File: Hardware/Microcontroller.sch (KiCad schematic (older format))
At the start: 28 parts

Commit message: Charger circuitry values
#26
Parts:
- removed C?: 4.7nF, symbol Capacitor
- removed D? (x2): TVS, symbol TVS
- removed R?: 1M, symbol Resistor
- removed RV? (x2): Varistor, symbol Varistor
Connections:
- net labels removed: GNDPWR
- wire segments 116 -> 77
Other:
- moved on the sheet: J?, PTC?

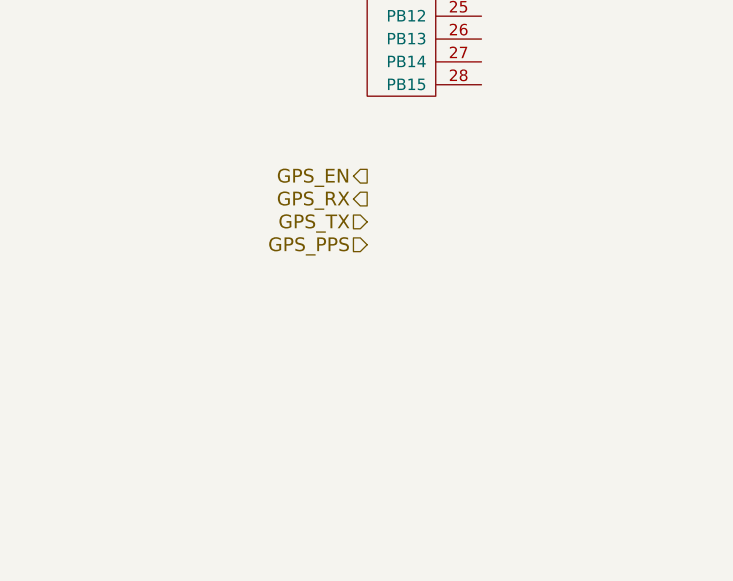
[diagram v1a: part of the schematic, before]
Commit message: Add solar charging capability
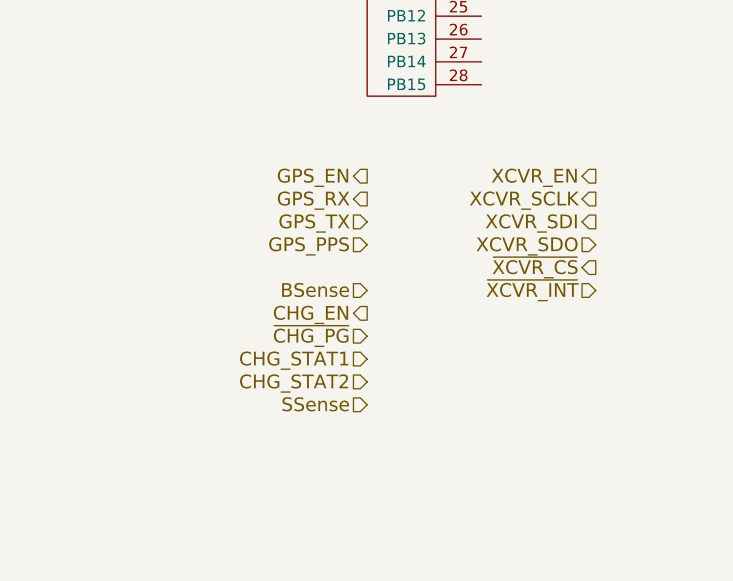
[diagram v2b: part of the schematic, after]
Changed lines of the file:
@@
 Wire Wire Line
 	4400 1400 4300 1400
+Text HLabel 8500 5500 0    60   Input ~ 0
+BSense
+Text HLabel 8500 5600 0    60   Output ~ 0
+CHG_EN
+Text HLabel 8500 5700 0    60   Input ~ 0
+~CHG_PG
+Text HLabel 8500 5800 0    60   Input ~ 0
+CHG_STAT1
+Text HLabel 8500 5900 0    60   Input ~ 0
+CHG_STAT2
+Text HLabel 9500 5000 0    60   Output ~ 0
+XCVR_EN
+Text HLabel 9500 5100 0    60   Output ~ 0
+XCVR_SCLK
+Text HLabel 9500 5200 0    60   Output ~ 0
+XCVR_SDI
+Text HLabel 9500 5300 0    60   Input ~ 0
+XCVR_SDO
+Text HLabel 9500 5400 0    60   Output ~ 0
+~XCVR_CS
+Text HLabel 9500 5500 0    60   Input ~ 0
+~XCVR_INT
+Text HLabel 8500 6000 0    60   Input ~ 0
+SSense
 $EndSCHEMATC

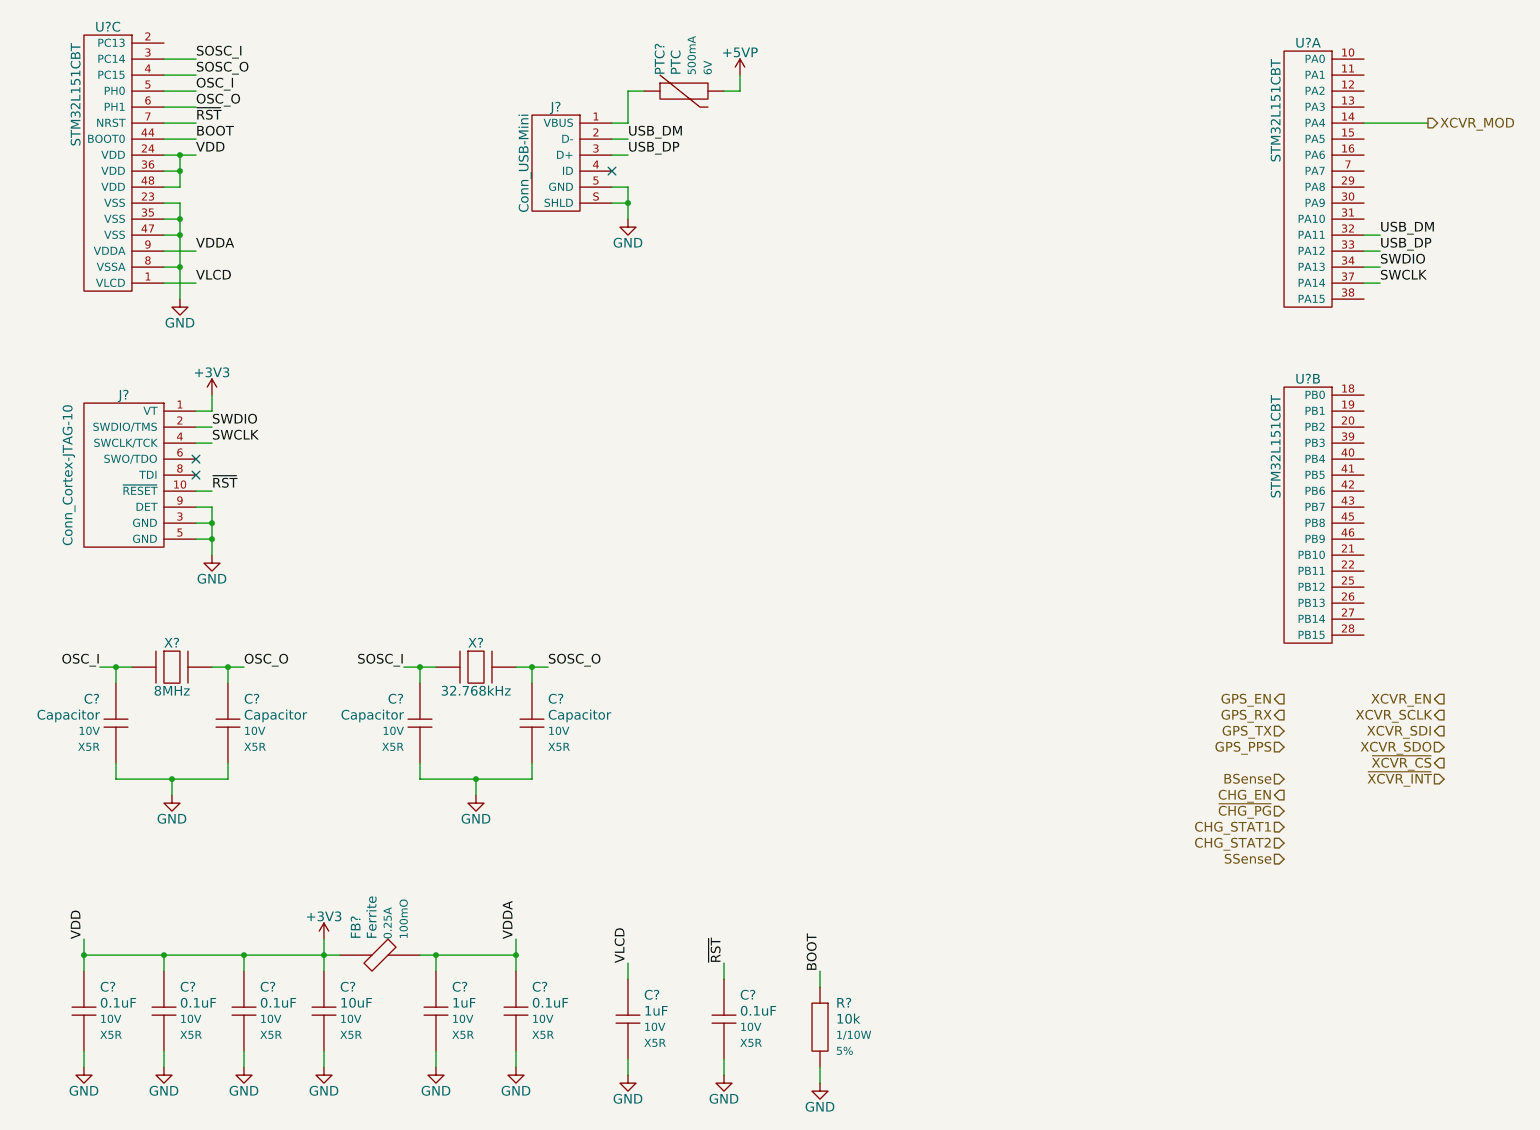
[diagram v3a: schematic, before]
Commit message: Oscillator selection
Closes #35
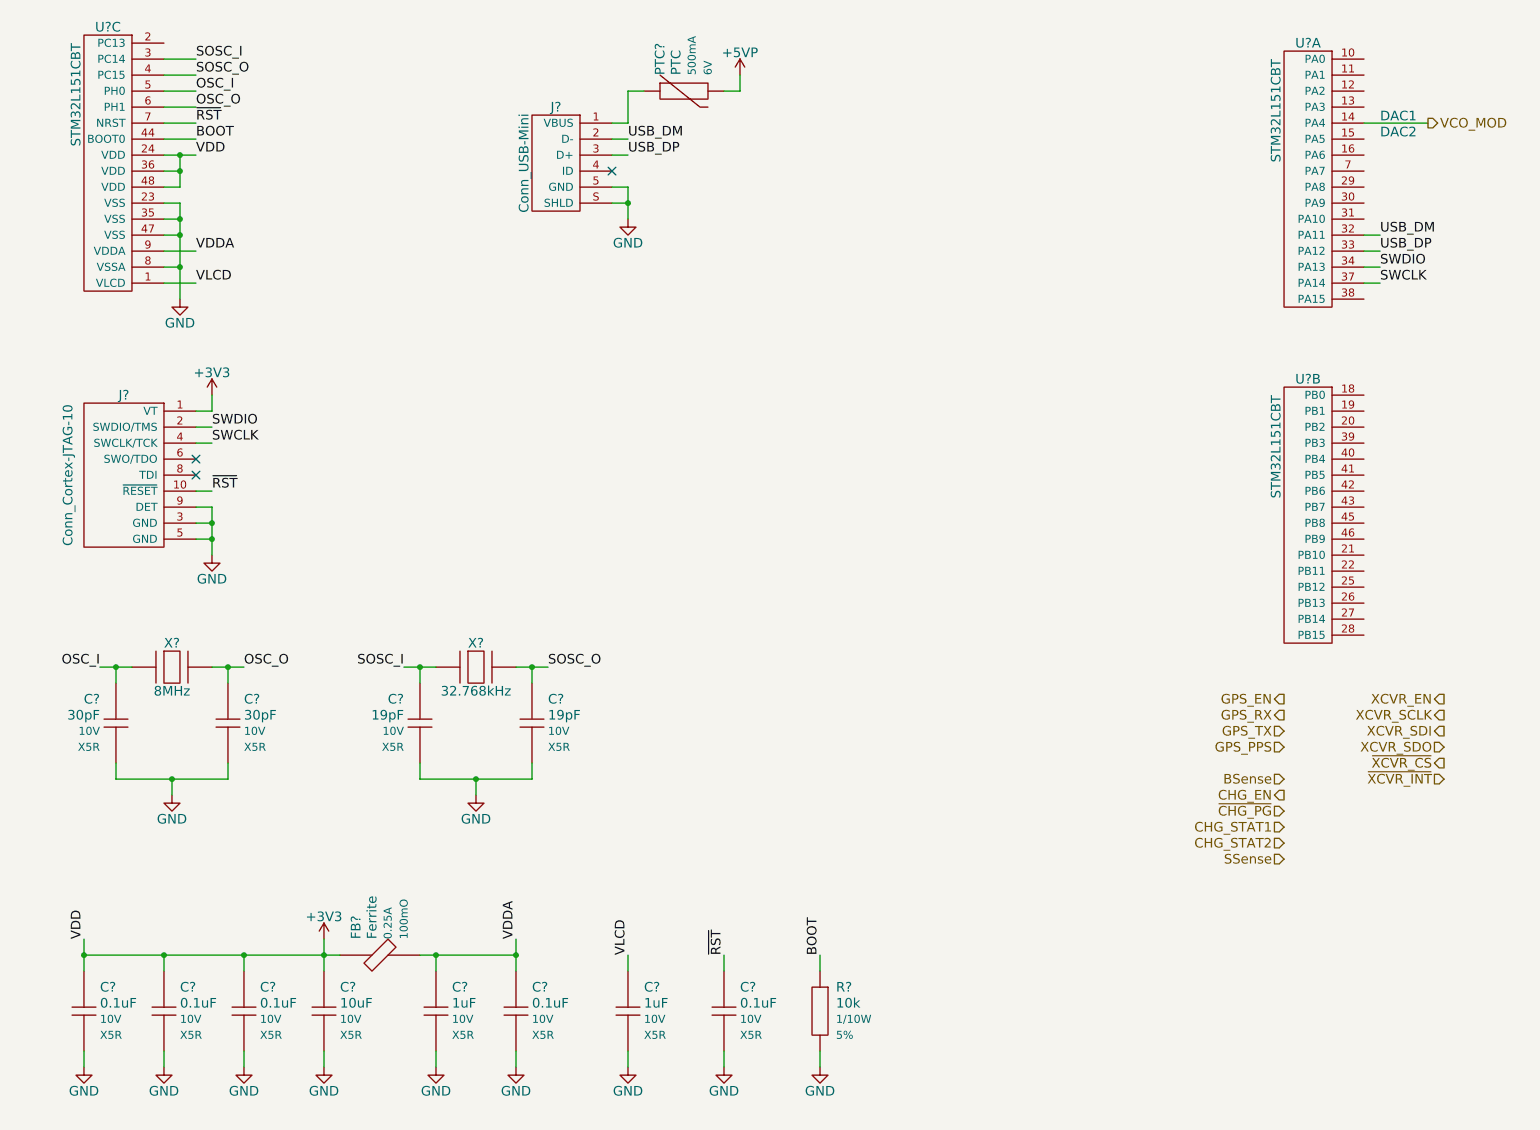
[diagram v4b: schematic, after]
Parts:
- C? (x2): value Capacitor -> 30pF
- C? (x2): value Capacitor -> 19pF
- X?: Manufacturer (none) -> Abracon; Manufacturer Part # (none) -> ABM3-8.000MHZ-D2Y-T; Vendor (none) -> Digikey; Vendor Part # (none) -> 535-10630-1-ND
- X?: Manufacturer (none) -> Abracon; Manufacturer Part # (none) -> ABS07-32.768KHZ-T; Vendor (none) -> Digikey; Vendor Part # (none) -> 535-9542-1-ND
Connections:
- net XCVR_MOD renamed VCO_MOD
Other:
- note added: "DAC1"
- note added: "DAC2"
- moved on the sheet: C?, R?
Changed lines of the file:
@@
 	1500 1100 1700 1100
 Text HLabel 9400 1400 2    60   Output ~ 0
-XCVR_MOD
+VCO_MOD
 Wire Wire Line
 	9400 1400 9000 1400
@@
 L Capacitor C?
 U 1 1 54979B61
-P 4400 7000
-F 0 "C?" V 4250 7100 60  0000 L CNN
-F 1 "1uF" V 4350 7100 60  0000 L CNN
-F 2 "" H 4300 7000 60  0001 C CNN
-F 3 "" H 4400 7100 60  0001 C CNN
-F 4 "Value" H 4400 7000 60  0001 C CNN "Manufacturer"
-F 5 "Value" H 4400 7000 60  0001 C CNN "Manufacturer Part #"
-F 6 "Value" H 4400 7000 60  0001 C CNN "Vendor"
-F 7 "Value" H 4400 7000 60  0001 C CNN "Vendor Part #"
-F 8 "10V" V 4450 7100 50  0000 L CNN "Voltage"
-F 9 "X5R" V 4550 7100 50  0000 L CNN "Dielectric"
-	1    4400 7000
+P 4400 6950
+F 0 "C?" V 4250 7050 60  0000 L CNN
+F 1 "1uF" V 4350 7050 60  0000 L CNN
+F 2 "" H 4300 6950 60  0001 C CNN
+F 3 "" H 4400 7050 60  0001 C CNN
+F 4 "Value" H 4400 6950 60  0001 C CNN "Manufacturer"
+F 5 "Value" H 4400 6950 60  0001 C CNN "Manufacturer Part #"
+F 6 "Value" H 4400 6950 60  0001 C CNN "Vendor"
+F 7 "Value" H 4400 6950 60  0001 C CNN "Vendor Part #"
+F 8 "10V" V 4450 7050 50  0000 L CNN "Voltage"
+F 9 "X5R" V 4550 7050 50  0000 L CNN "Dielectric"
+	1    4400 6950
 	0    1    1    0
 $EndComp
@@
 F 2 "" H 1550 4800 60  0000 C CNN
 F 3 "" H 1550 4800 60  0000 C CNN
+F 4 "Abracon" H 1550 4800 60  0001 C CNN "Manufacturer"
+F 5 "ABM3-8.000MHZ-D2Y-T" H 1550 4800 60  0001 C CNN "Manufacturer Part #"
+F 6 "Digikey" H 1550 4800 60  0001 C CNN "Vendor"
+F 7 "535-10630-1-ND" H 1550 4800 60  0001 C CNN "Vendor Part #"
 	1    1550 4800
 	1    0    0    -1
@@
 F 2 "" H 3450 4800 60  0000 C CNN
 F 3 "" H 3450 4800 60  0000 C CNN
+F 4 "Abracon" H 3450 4800 60  0001 C CNN "Manufacturer"
+F 5 "ABS07-32.768KHZ-T" H 3450 4800 60  0001 C CNN "Manufacturer Part #"
+F 6 "Digikey" H 3450 4800 60  0001 C CNN "Vendor"
+F 7 "535-9542-1-ND" H 3450 4800 60  0001 C CNN "Vendor Part #"
 	1    3450 4800
 	1    0    0    -1
@@
 P 1900 5150
 F 0 "C?" V 1750 5250 60  0000 L CNN
-F 1 "Capacitor" V 1850 5250 60  0000 L CNN
+F 1 "30pF" V 1850 5250 60  0000 L CNN
 F 2 "" H 1800 5150 60  0001 C CNN
 F 3 "" H 1900 5250 60  0001 C CNN
@@
 P 1200 5150
 F 0 "C?" V 1050 5250 60  0000 L CNN
-F 1 "Capacitor" V 1150 5250 60  0000 L CNN
+F 1 "30pF" V 1150 5250 60  0000 L CNN
 F 2 "" H 1100 5150 60  0001 C CNN
 F 3 "" H 1200 5250 60  0001 C CNN
@@
 P 3100 5150
 F 0 "C?" V 2950 5250 60  0000 L CNN
-F 1 "Capacitor" V 3050 5250 60  0000 L CNN
+F 1 "19pF" V 3050 5250 60  0000 L CNN
 F 2 "" H 3000 5150 60  0001 C CNN
 F 3 "" H 3100 5250 60  0001 C CNN
@@
 P 3800 5150
 F 0 "C?" V 3650 5250 60  0000 L CNN
-F 1 "Capacitor" V 3750 5250 60  0000 L CNN
+F 1 "19pF" V 3750 5250 60  0000 L CNN
 F 2 "" H 3700 5150 60  0001 C CNN
 F 3 "" H 3800 5250 60  0001 C CNN
@@
 L GND #PWR?
 U 1 1 5497E456
-P 4400 7350
-F 0 "#PWR?" H 4400 7100 60  0001 C CNN
-F 1 "GND" H 4400 7200 60  0000 C CNN
-F 2 "" H 4400 7350 60  0000 C CNN
-F 3 "" H 4400 7350 60  0000 C CNN
-	1    4400 7350
-	1    0    0    -1
-$EndComp
-Wire Wire Line
-	4400 7350 4400 7250
+P 4400 7300
+F 0 "#PWR?" H 4400 7050 60  0001 C CNN
+F 1 "GND" H 4400 7150 60  0000 C CNN
+F 2 "" H 4400 7300 60  0000 C CNN
+F 3 "" H 4400 7300 60  0000 C CNN
+	1    4400 7300
+	1    0    0    -1
+$EndComp
+Wire Wire Line
+	4400 7300 4400 7200
 $Comp
 L Capacitor C?
 U 1 1 5497E4E3
-P 5000 7000
-F 0 "C?" V 4850 7100 60  0000 L CNN
-F 1 "0.1uF" V 4950 7100 60  0000 L CNN
-F 2 "" H 4900 7000 60  0001 C CNN
-F 3 "" H 5000 7100 60  0001 C CNN
-F 4 "Value" H 5000 7000 60  0001 C CNN "Manufacturer"
-F 5 "Value" H 5000 7000 60  0001 C CNN "Manufacturer Part #"
-F 6 "Value" H 5000 7000 60  0001 C CNN "Vendor"
-F 7 "Value" H 5000 7000 60  0001 C CNN "Vendor Part #"
-F 8 "10V" V 5050 7100 50  0000 L CNN "Voltage"
-F 9 "X5R" V 5150 7100 50  0000 L CNN "Dielectric"
-	1    5000 7000
+P 5000 6950
+F 0 "C?" V 4850 7050 60  0000 L CNN
+F 1 "0.1uF" V 4950 7050 60  0000 L CNN
+F 2 "" H 4900 6950 60  0001 C CNN
+F 3 "" H 5000 7050 60  0001 C CNN
+F 4 "Value" H 5000 6950 60  0001 C CNN "Manufacturer"
+F 5 "Value" H 5000 6950 60  0001 C CNN "Manufacturer Part #"
+F 6 "Value" H 5000 6950 60  0001 C CNN "Vendor"
+F 7 "Value" H 5000 6950 60  0001 C CNN "Vendor Part #"
+F 8 "10V" V 5050 7050 50  0000 L CNN "Voltage"
+F 9 "X5R" V 5150 7050 50  0000 L CNN "Dielectric"
+	1    5000 6950
 	0    1    1    0
 $EndComp
@@
 L GND #PWR?
 U 1 1 5497E541
-P 5000 7350
-F 0 "#PWR?" H 5000 7100 60  0001 C CNN
-F 1 "GND" H 5000 7200 60  0000 C CNN
-F 2 "" H 5000 7350 60  0000 C CNN
-F 3 "" H 5000 7350 60  0000 C CNN
-	1    5000 7350
-	1    0    0    -1
-$EndComp
-Text Label 4400 6650 1    60   ~ 0
+P 5000 7300
+F 0 "#PWR?" H 5000 7050 60  0001 C CNN
+F 1 "GND" H 5000 7150 60  0000 C CNN
+F 2 "" H 5000 7300 60  0000 C CNN
+F 3 "" H 5000 7300 60  0000 C CNN
+	1    5000 7300
+	1    0    0    -1
+$EndComp
+Text Label 4400 6600 1    60   ~ 0
 VLCD
-Text Label 5000 6650 1    60   ~ 0
+Text Label 5000 6600 1    60   ~ 0
 ~RST
 Wire Wire Line
-	5000 6650 5000 6750
-Wire Wire Line
-	4400 6650 4400 6750
-Wire Wire Line
-	5000 7350 5000 7250
+	5000 6600 5000 6700
+Wire Wire Line
+	4400 6600 4400 6700
+Wire Wire Line
+	5000 7300 5000 7200
 Wire Wire Line
 	1500 1900 1600 1900
@@
 L Resistor R?
 U 1 1 54980C1B
-P 5600 7050
-F 0 "R?" V 5450 7150 60  0000 L CNN
-F 1 "10k" V 5550 7150 60  0000 L CNN
-F 2 "" H 5500 7050 60  0001 C CNN
-F 3 "" H 5600 7150 60  0001 C CNN
-F 4 "Value" H 5600 7050 60  0001 C CNN "Manufacturer"
-F 5 "Value" H 5600 7050 60  0001 C CNN "Manufacturer Part #"
-F 6 "Value" H 5600 7050 60  0001 C CNN "Vendor"
-F 7 "Value" H 5600 7050 60  0001 C CNN "Vendor Part #"
-F 8 "1/10W" V 5650 7150 50  0000 L CNN "Power"
-F 9 "5%" V 5750 7150 50  0000 L CNN "Tolerance"
-	1    5600 7050
+P 5600 6950
+F 0 "R?" V 5450 7050 60  0000 L CNN
+F 1 "10k" V 5550 7050 60  0000 L CNN
+F 2 "" H 5500 6950 60  0001 C CNN
+F 3 "" H 5600 7050 60  0001 C CNN
+F 4 "Value" H 5600 6950 60  0001 C CNN "Manufacturer"
+F 5 "Value" H 5600 6950 60  0001 C CNN "Manufacturer Part #"
+F 6 "Value" H 5600 6950 60  0001 C CNN "Vendor"
+F 7 "Value" H 5600 6950 60  0001 C CNN "Vendor Part #"
+F 8 "1/10W" V 5650 7050 50  0000 L CNN "Power"
+F 9 "5%" V 5750 7050 50  0000 L CNN "Tolerance"
+	1    5600 6950
 	0    1    1    0
 $EndComp
@@
 L GND #PWR?
 U 1 1 54980CDC
-P 5600 7400
-F 0 "#PWR?" H 5600 7150 60  0001 C CNN
-F 1 "GND" H 5600 7250 60  0000 C CNN
-F 2 "" H 5600 7400 60  0000 C CNN
-F 3 "" H 5600 7400 60  0000 C CNN
-	1    5600 7400
-	1    0    0    -1
-$EndComp
-Wire Wire Line
-	5600 7300 5600 7400
-Text Label 5600 6700 1    60   ~ 0
+P 5600 7300
+F 0 "#PWR?" H 5600 7050 60  0001 C CNN
+F 1 "GND" H 5600 7150 60  0000 C CNN
+F 2 "" H 5600 7300 60  0000 C CNN
+F 3 "" H 5600 7300 60  0000 C CNN
+	1    5600 7300
+	1    0    0    -1
+$EndComp
+Wire Wire Line
+	5600 7200 5600 7300
+Text Label 5600 6600 1    60   ~ 0
 BOOT
 Wire Wire Line
-	5600 6700 5600 6800
+	5600 6600 5600 6700
 Text Label 9100 2100 0    60   ~ 0
 USB_DM
@@
 Text HLabel 8500 6000 0    60   Input ~ 0
 SSense
+Text Notes 9100 1400 0    60   ~ 0
+DAC1
+Text Notes 9100 1500 0    60   ~ 0
+DAC2
 $EndSCHEMATC

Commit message: Update general layout
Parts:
- added D? (x2): LED, symbol LED
- added R? (x2): Resistor, symbol Resistor
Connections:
- net +3V3: now also R?.1, R?.1
- new net: D?.A, R?.2 (x2)
- new net LED0: D?.C
- new net LED1: D?.C
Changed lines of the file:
@@
 Text Notes 9100 1500 0    60   ~ 0
 DAC2
+$Comp
+L LED D?
+U 1 1 54A1A4D6
+P 5150 3300
+F 0 "D?" V 5000 3400 60  0000 L CNN
+F 1 "LED" V 5100 3400 60  0000 L CNN
+F 2 "" H 5150 3300 60  0000 C CNN
+F 3 "" H 5150 3300 60  0000 C CNN
+F 4 "Value" H 5150 3300 60  0001 C CNN "Manufacturer"
+F 5 "Value" H 5150 3300 60  0001 C CNN "Manufacturer Part #"
+F 6 "Value" H 5150 3300 60  0001 C CNN "Vendor"
+F 7 "Value" H 5150 3300 60  0001 C CNN "Vendor Part #"
+F 8 "Vf" V 5200 3400 60  0000 L CNN "Forward Voltage"
+F 9 "I" V 5300 3400 60  0000 L CNN "Current"
+	1    5150 3300
+	1    0    0    -1
+$EndComp
+$Comp
+L LED D?
+U 1 1 54A1A544
+P 5150 3700
+F 0 "D?" V 5000 3800 60  0000 L CNN
+F 1 "LED" V 5100 3800 60  0000 L CNN
+F 2 "" H 5150 3700 60  0000 C CNN
+F 3 "" H 5150 3700 60  0000 C CNN
+F 4 "Value" H 5150 3700 60  0001 C CNN "Manufacturer"
+F 5 "Value" H 5150 3700 60  0001 C CNN "Manufacturer Part #"
+F 6 "Value" H 5150 3700 60  0001 C CNN "Vendor"
+F 7 "Value" H 5150 3700 60  0001 C CNN "Vendor Part #"
+F 8 "Vf" V 5200 3800 60  0000 L CNN "Forward Voltage"
+F 9 "I" V 5300 3800 60  0000 L CNN "Current"
+	1    5150 3700
+	1    0    0    -1
+$EndComp
+$Comp
+L Resistor R?
+U 1 1 54A1A58D
+P 4550 3300
+F 0 "R?" V 4400 3400 60  0000 L CNN
+F 1 "Resistor" V 4500 3400 60  0000 L CNN
+F 2 "" H 4450 3300 60  0001 C CNN
+F 3 "" H 4550 3400 60  0001 C CNN
+F 4 "Value" H 4550 3300 60  0001 C CNN "Manufacturer"
+F 5 "Value" H 4550 3300 60  0001 C CNN "Manufacturer Part #"
+F 6 "Value" H 4550 3300 60  0001 C CNN "Vendor"
+F 7 "Value" H 4550 3300 60  0001 C CNN "Vendor Part #"
+F 8 "1/10W" V 4600 3400 50  0000 L CNN "Power"
+F 9 "5%" V 4700 3400 50  0000 L CNN "Tolerance"
+	1    4550 3300
+	1    0    0    -1
+$EndComp
+$Comp
+L Resistor R?
+U 1 1 54A1A5F4
+P 4550 3700
+F 0 "R?" V 4400 3800 60  0000 L CNN
+F 1 "Resistor" V 4500 3800 60  0000 L CNN
+F 2 "" H 4450 3700 60  0001 C CNN
+F 3 "" H 4550 3800 60  0001 C CNN
+F 4 "Value" H 4550 3700 60  0001 C CNN "Manufacturer"
+F 5 "Value" H 4550 3700 60  0001 C CNN "Manufacturer Part #"
+F 6 "Value" H 4550 3700 60  0001 C CNN "Vendor"
+F 7 "Value" H 4550 3700 60  0001 C CNN "Vendor Part #"
+F 8 "1/10W" V 4600 3800 50  0000 L CNN "Power"
+F 9 "5%" V 4700 3800 50  0000 L CNN "Tolerance"
+	1    4550 3700
+	1    0    0    -1
+$EndComp
+$Comp
+L +3V3 #PWR?
+U 1 1 54A1A643
+P 4200 3200
+F 0 "#PWR?" H 4200 3050 60  0001 C CNN
+F 1 "+3V3" H 4200 3340 60  0000 C CNN
+F 2 "" H 4200 3200 60  0000 C CNN
+F 3 "" H 4200 3200 60  0000 C CNN
+	1    4200 3200
+	1    0    0    -1
+$EndComp
+Wire Wire Line
+	4200 3200 4200 3700
+Wire Wire Line
+	4200 3700 4300 3700
+Wire Wire Line
+	4300 3300 4200 3300
+Connection ~ 4200 3300
+Text Label 5500 3300 0    60   ~ 0
+LED0
+Text Label 5500 3700 0    60   ~ 0
+LED1
+Wire Wire Line
+	4800 3300 4900 3300
+Wire Wire Line
+	4800 3700 4900 3700
+Wire Wire Line
+	5400 3300 5500 3300
+Wire Wire Line
+	5400 3700 5500 3700
 $EndSCHEMATC

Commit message: Power sheet BOM fields
Remove annotations
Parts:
- gave numbers to parts that had none: 24

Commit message: BOM fields
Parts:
- C11, C14: value 19pF -> 18pF; Dielectric X5R -> NP0; Manufacturer Value -> Samsung; Manufacturer Part # Value -> CL10C180JB8NNNC; Vendor Value -> Digikey; Vendor Part # Value -> 1276-1089-1-ND; Voltage 10V -> 50V
- C12, C15: Dielectric X5R -> X7R; Manufacturer Value -> Samsung; Manufacturer Part # Value -> CL10B105KP8NNNC; Vendor Value -> Digikey; Vendor Part # Value -> 1276-1946-1-ND
- C13, C16, C5, C7, C9: Dielectric X5R -> X7R; Manufacturer Value -> Samsung; Manufacturer Part # Value -> CL10B104KO8NNNC; Vendor Value -> Digikey; Vendor Part # Value -> 1276-1005-1-ND; Voltage 10V -> 16V
- C6, C8: Dielectric X5R -> NP0; Manufacturer Value -> Samsung; Manufacturer Part # Value -> CL10C300JB8NNNC; Vendor Value -> Digikey; Vendor Part # Value -> 1276-1021-1-ND; Voltage 10V -> 50V
- R5: value 10k -> 100k; Manufacturer Value -> Yageo; Manufacturer Part # Value -> RC0603JR-07100KL; Vendor Value -> Digikey; Vendor Part # Value -> 311-100KGRCT-ND
